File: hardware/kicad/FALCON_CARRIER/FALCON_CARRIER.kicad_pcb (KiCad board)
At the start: 2 copper layers, 165 x 125 mm, 55 parts, among them J1 B2P-VH-FB-B, J10 BM03B-GHS-TBT, J11 470531000, J12 BM04B-GHS-TBT, J13 470531000, J2 BM04B-GHS-TBT, J3 GPS_UART, J4 INA260_BAT_LOGIC, J5 INA260_SOLAR_0X41, J6 BM04B-GHS-TBT, J7 BM03B-GHS-TBT, J8 BM03B-GHS-TBT, J9 BM03B-GHS-TBT, Q1 2N7002_FAN1_PWM, Q2 2N7002_FAN2_PWM, U1 AP2112K-3.3TRG1, U2 ESP32-DevKitC_V4_WROOM-32E, U3 BNO085_SPI, U4 ADS1115_0X48, U6 EFUSE_TPS25947_TBD

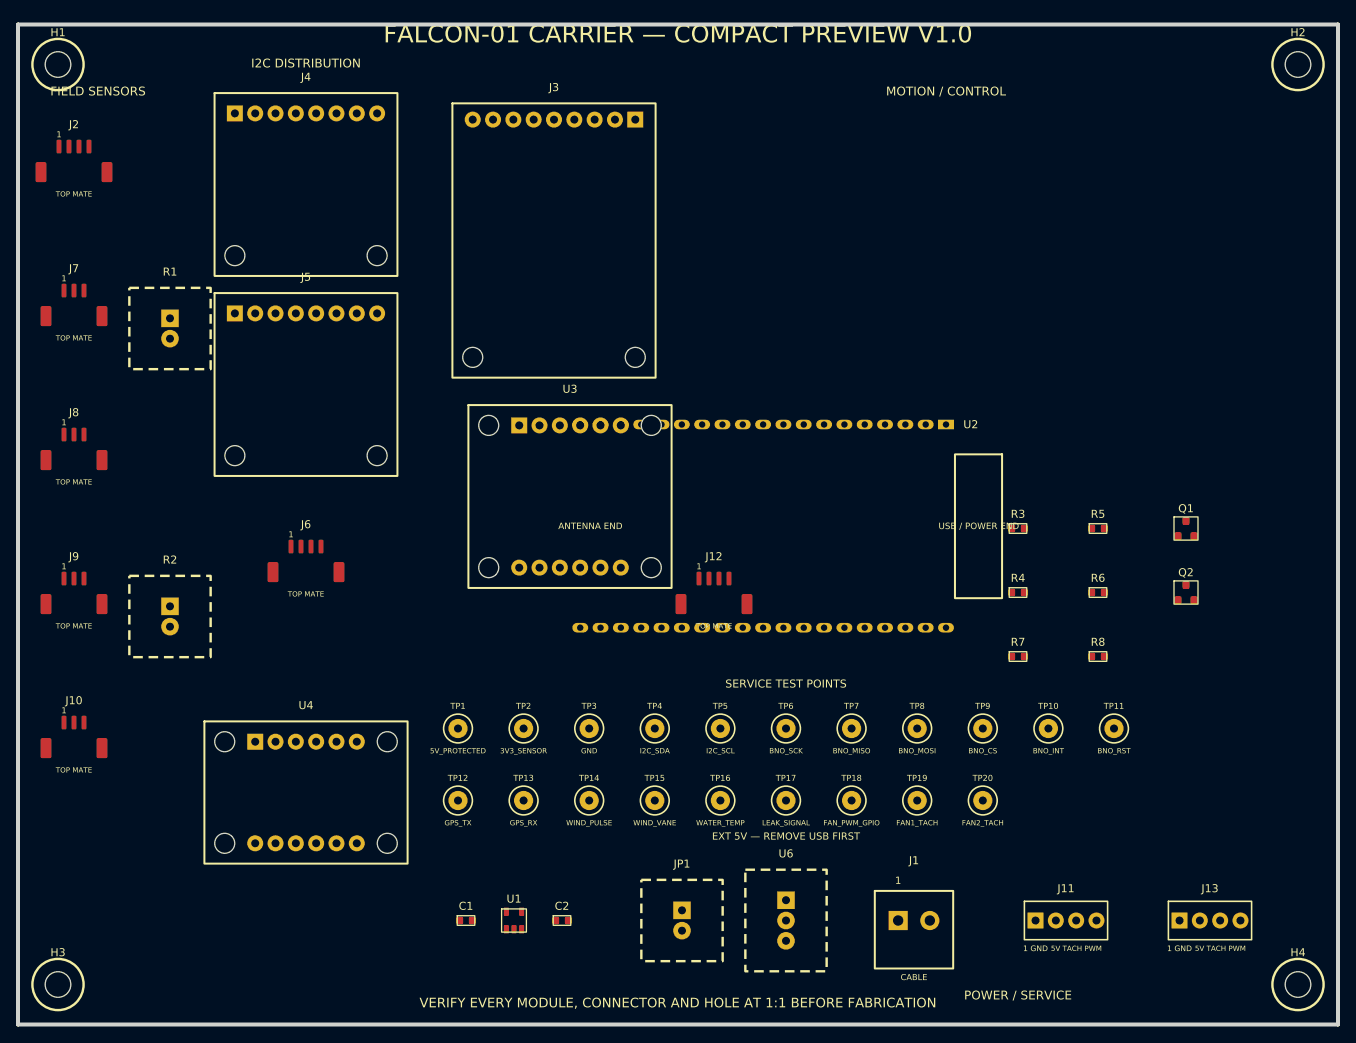
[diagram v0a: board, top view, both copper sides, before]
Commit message: Complete presentation PCB electronics models
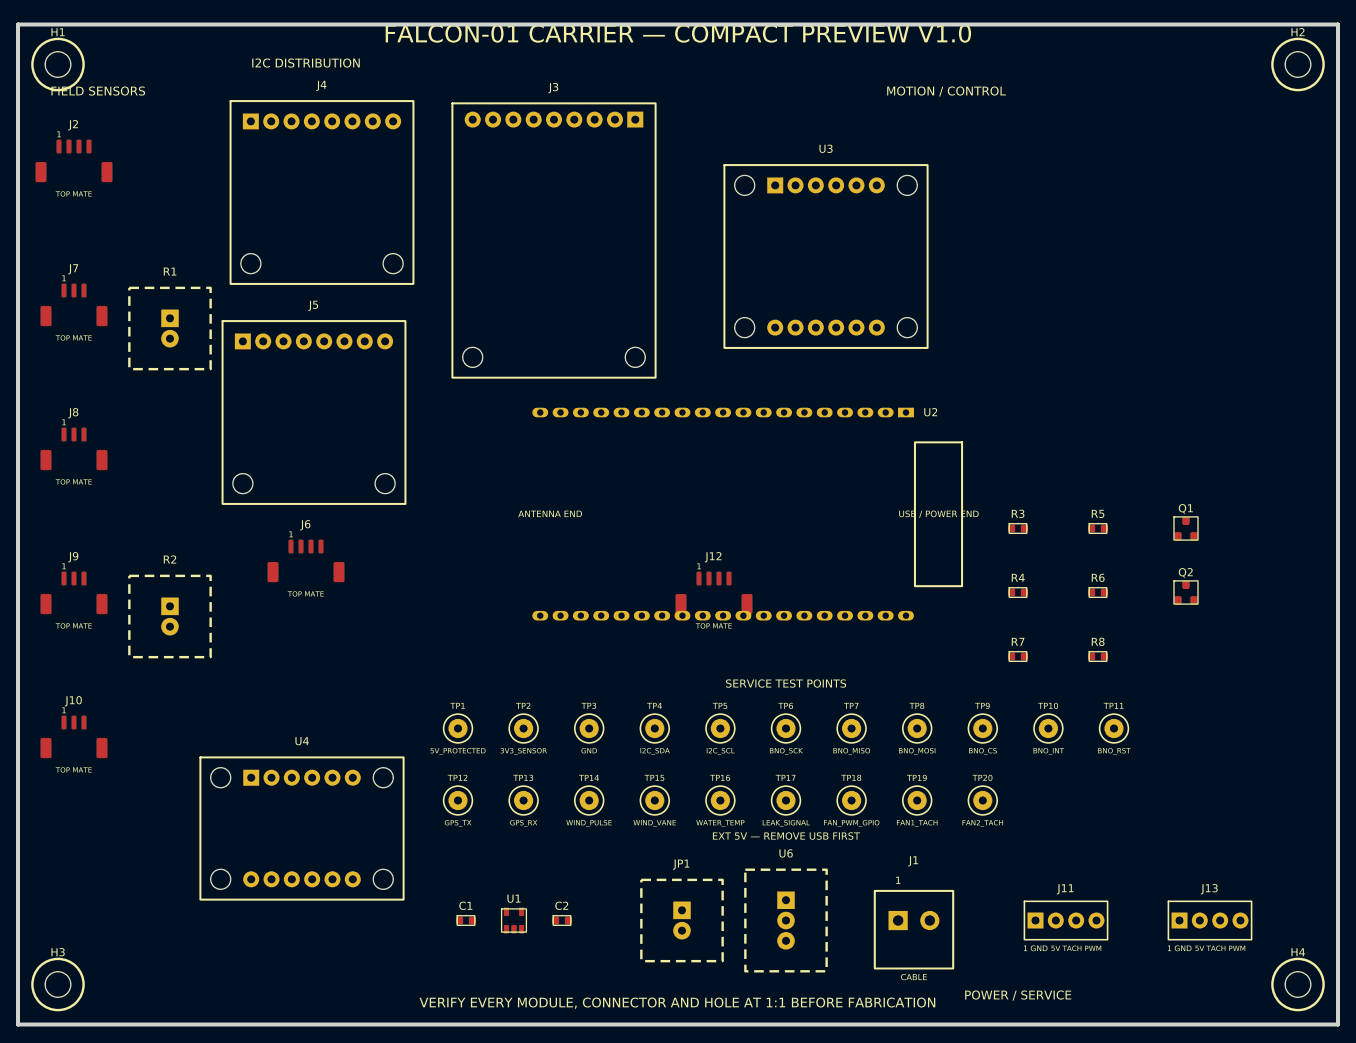
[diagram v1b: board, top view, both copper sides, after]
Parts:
- moved U3 43.9 mm to (121.0, 49.0)
- moved U2 5.22 mm to (131.0, 68.5)
- moved U4 4.53 mm to (55.5, 120.5)
- moved J5 3.64 mm to (57.0, 68.5)
- moved J4 2.24 mm to (58.0, 41.0)
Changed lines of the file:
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@@
 	(footprint "FALCON_LOCKED_ADS1115_0X48"
 		(layer "F.Cu")
-		(at 56 116)
+		(at 55.5 120.5)
 		(descr "Adafruit ADS1115 PID 1085 STEMMA QT official Eagle CAD; receiving check still required")
 		(tags "FALCON MANUFACTURER CAD SOCKET")
@@
 	(footprint "FALCON_LOCKED_INA260_SOLAR_0X41"
 		(layer "F.Cu")
-		(at 56 65)
+		(at 57 68.5)
 		(descr "Adafruit INA260 PID 4226 official Eagle CAD; receiving check still required")
 		(tags "FALCON MANUFACTURER CAD SOCKET")
@@
 	(footprint "FALCON_LOCKED_BNO085_SPI"
 		(layer "F.Cu")
-		(at 89 79)
+		(at 121 49)
 		(descr "Adafruit BNO08x Rev C official Eagle CAD; receiving check still required")
 		(tags "FALCON MANUFACTURER CAD SOCKET")
@@
 		)
 		(embedded_fonts no)
-		(model "${KIPRJMOD}/models/resistor_0603.wrl"
+		(model "${KIPRJMOD}/models/capacitor_0603.wrl"
 			(offset
 				(xyz 0 0 0)
@@
 	(footprint "FALCON_LOCKED_ESP32_DEVKITC_V4"
 		(layer "F.Cu")
-		(at 136 70 -90)
+		(at 131 68.5 -90)
 		(descr "ESP32-DevKitC V4 geometry locked from official Espressif KiCad library")
 		(tags "ESP32 DevKitC V4 WROOM-32E OFFICIAL GEOMETRY")
@@
 		)
 		(embedded_fonts no)
-		(model "${KIPRJMOD}/models/resistor_0603.wrl"
+		(model "${KIPRJMOD}/models/capacitor_0603.wrl"
 			(offset
 				(xyz 0 0 0)
@@
 	(footprint "FALCON_LOCKED_INA260_BAT_LOGIC"
 		(layer "F.Cu")
-		(at 56 40)
+		(at 58 41)
 		(descr "Adafruit INA260 PID 4226 official Eagle CAD; receiving check still required")
 		(tags "FALCON MANUFACTURER CAD SOCKET")
@@
 		)
 		(embedded_fonts no)
-		(model "${KIPRJMOD}/models/module_generic.wrl"
+		(model "${KIPRJMOD}/models/power_protection_preview.wrl"
 			(offset
 				(xyz 0 0 0)
@@
 		)
 		(embedded_fonts no)
-		(model "${KIPRJMOD}/models/module_generic.wrl"
+		(model "${KIPRJMOD}/models/jumper_2pin.wrl"
 			(offset
 				(xyz 0 0 0)

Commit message: Lock field connector orientation labels
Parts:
- moved J12 60.0 mm to (153.6, 56.2)
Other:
- board text added: "1:+ 2:LEAK 3:G"
- board text added: "1:+ 2:PULSE 3:G"
- board text added: "1:+ 2:SCL 3:SDA 4:G"
- board text added: "1:+ 2:TEMP 3:G"
- board text added: "1:+ 2:VANE 3:G"
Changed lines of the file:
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@@
 	(footprint "JST_GH_04P_TOP_BM04B-GHS-TBT"
 		(layer "F.Cu")
-		(at 107 94)
+		(at 153.625 56.25)
 		(descr "JST BM04B-GHS-TBT official-catalog top-entry SMT land pattern")
 		(tags "JST GH 1.25MM TOP ENTRY OFFICIAL CATALOG")
@@
 	)
 	(gr_text "FALCON-01 CARRIER — COMPACT PREVIEW V1.0"
-		(at 102.5 22.5 0)
+		(at 108.5 25 0)
 		(layer "F.SilkS")
 		(effects
@@
 		)
 	)
+	(gr_text "1:+  2:SCL  3:SDA  4:G"
+		(at 34.5 44.5 0)
+		(layer "F.SilkS")
+		(effects (font (size 0.58 0.58) (thickness 0.11)) (justify left bottom))
+	)
+	(gr_text "1:+  2:PULSE  3:G"
+		(at 34.5 62.5 0)
+		(layer "F.SilkS")
+		(effects (font (size 0.58 0.58) (thickness 0.11)) (justify left bottom))
+	)
+	(gr_text "1:+  2:VANE  3:G"
+		(at 34.5 80.5 0)
+		(layer "F.SilkS")
+		(effects (font (size 0.58 0.58) (thickness 0.11)) (justify left bottom))
+	)
+	(gr_text "1:+  2:TEMP  3:G"
+		(at 34.5 98.5 0)
+		(layer "F.SilkS")
+		(effects (font (size 0.58 0.58) (thickness 0.11)) (justify left bottom))
+	)
+	(gr_text "1:+  2:LEAK  3:G"
+		(at 34.5 116.5 0)
+		(layer "F.SilkS")
+		(effects (font (size 0.58 0.58) (thickness 0.11)) (justify left bottom))
+	)
 	(embedded_fonts no)

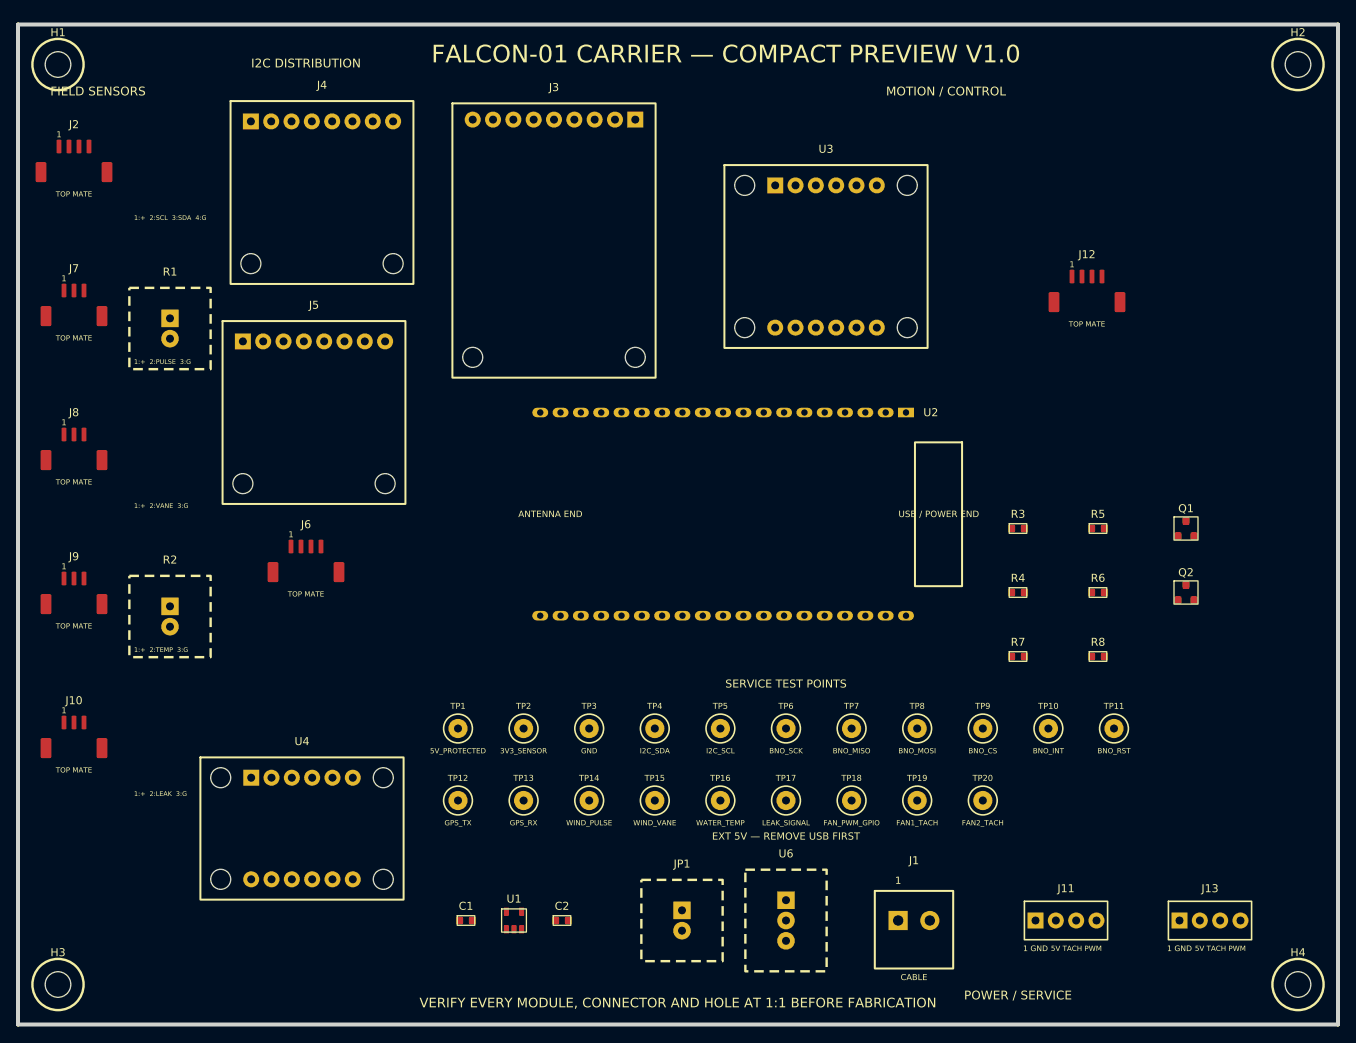
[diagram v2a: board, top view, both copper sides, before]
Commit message: Reorganize PCB into industrial functional zones
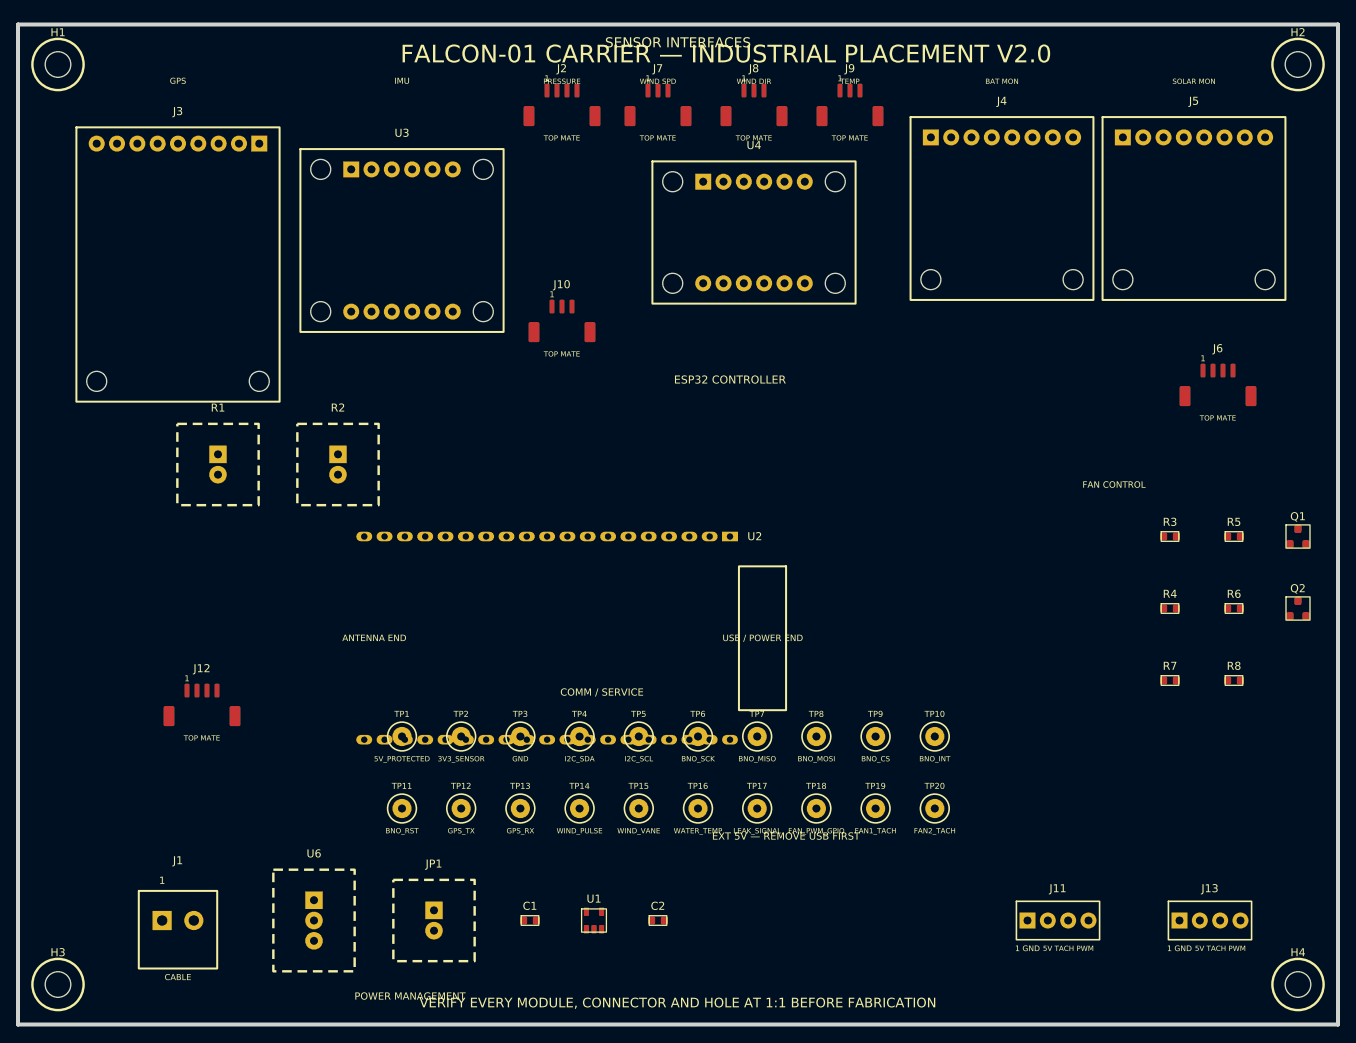
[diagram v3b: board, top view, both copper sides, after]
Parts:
- moved J12 122.1 mm to (43.0, 108.0)
- moved J6 116.1 mm to (170.0, 68.0)
- moved J9 114.6 mm to (124.0, 33.0)
- moved J5 112.9 mm to (167.0, 43.0)
- moved J8 95.3 mm to (112.0, 33.0)
- moved U4 93.5 mm to (112.0, 46.0)
- moved J1 92.0 mm to (40.0, 132.0)
- moved TP11 89.6 mm to (68.0, 118.0)
- moved J4 85.0 mm to (143.0, 43.0)
- moved J10 80.2 mm to (88.0, 60.0)
- moved J7 77.2 mm to (100.0, 33.0)
- moved J2 61.4 mm to (88.0, 33.0)
- moved U6 59.0 mm to (57.0, 132.0)
- moved U3 53.0 mm to (68.0, 47.0)
- moved J3 47.1 mm to (40.0, 50.0)
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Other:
- board text added: "BAT MON"
- board text added: "COMM / SERVICE"
- board text added: "ESP32 CONTROLLER"
- board text added: "FALCON-01 CARRIER — INDUSTRIAL PLACEMENT V2.0"
- board text added: "FAN CONTROL"
- board text added: "GPS"
- board text added: "IMU"
- board text added: "POWER MANAGEMENT"
- board text added: "PRESSURE"
- board text added: "SENSOR INTERFACES"
- board text added: "SOLAR MON"
- board text added: "TEMP"
- board text added: "WIND DIR"
- board text added: "WIND SPD"
- board text removed: "1:+ 2:LEAK 3:G"
- board text removed: "1:+ 2:PULSE 3:G"
- board text removed: "1:+ 2:SCL 3:SDA 4:G"
- board text removed: "1:+ 2:TEMP 3:G"
- board text removed: "1:+ 2:VANE 3:G"
- board text removed: "FALCON-01 CARRIER — COMPACT PREVIEW V1.0"
- board text removed: "FIELD SENSORS"
- board text removed: "I2C DISTRIBUTION"
- board text removed: "MOTION / CONTROL"
- board text removed: "POWER / SERVICE"
- board text removed: "SERVICE TEST POINTS"
